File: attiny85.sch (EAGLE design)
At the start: 9 parts, among them U2 ATTINY85V-10SU

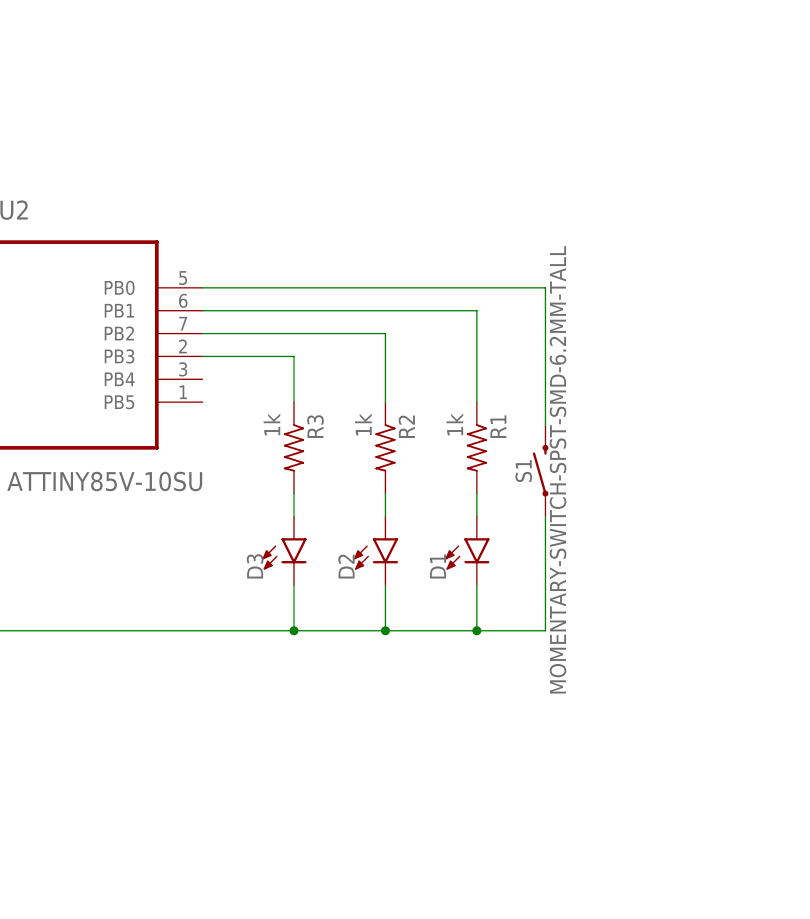
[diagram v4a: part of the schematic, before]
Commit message: Switching to using the "3" PWMs for the LEDs
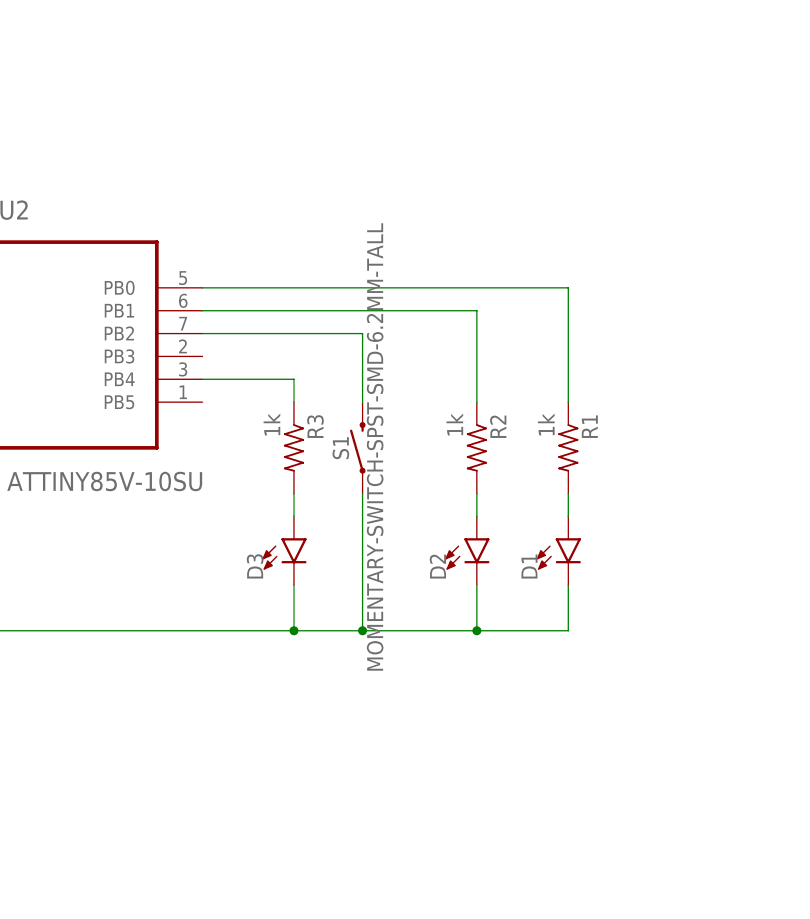
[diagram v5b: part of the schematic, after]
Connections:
- removed net N$8: R3.1, U2.PB3
- new net N$6: R3.1, U2.PB4
- net N$3: now also R1.1; no longer S1.2
- net N$4: now also R2.1; no longer R1.1
- net N$7: now also S1.2; no longer R2.1
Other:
- moved on the sheet: D1, D2, R1, R2, S1
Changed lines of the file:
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@@
 <instance part="FRAME1" gate="G$1" x="0" y="0"/>
 <instance part="FRAME1" gate="G$2" x="299.72" y="0"/>
-<instance part="R2" gate="G$1" x="93.98" y="185.42" rot="R270"/>
-<instance part="D2" gate="G$1" x="93.98" y="175.26"/>
+<instance part="R2" gate="G$1" x="104.14" y="185.42" rot="R270"/>
+<instance part="D2" gate="G$1" x="104.14" y="175.26"/>
 <instance part="R3" gate="G$1" x="83.82" y="185.42" rot="R270"/>
 <instance part="D3" gate="G$1" x="83.82" y="175.26"/>
 <instance part="BAT1" gate="G$1" x="30.48" y="198.12" rot="R90"/>
 <instance part="U2" gate="A" x="55.88" y="200.66"/>
-<instance part="R1" gate="G$1" x="104.14" y="185.42" rot="R270"/>
-<instance part="D1" gate="G$1" x="104.14" y="175.26"/>
-<instance part="S1" gate="G$1" x="111.76" y="182.88" rot="R90"/>
+<instance part="R1" gate="G$1" x="114.3" y="185.42" rot="R270"/>
+<instance part="D1" gate="G$1" x="114.3" y="175.26"/>
+<instance part="S1" gate="G$1" x="91.44" y="185.42" rot="R90"/>
 </instances>
 <busses>
@@
 <pinref part="R2" gate="G$1" pin="2"/>
 <pinref part="D2" gate="G$1" pin="A"/>
-<wire x1="93.98" y1="180.34" x2="93.98" y2="177.8" width="0.1524" layer="91"/>
+<wire x1="104.14" y1="180.34" x2="104.14" y2="177.8" width="0.1524" layer="91"/>
 </segment>
 </net>
@@
 <junction x="30.48" y="193.04"/>
 <pinref part="D1" gate="G$1" pin="C"/>
-<wire x1="104.14" y1="170.18" x2="104.14" y2="165.1" width="0.1524" layer="91"/>
+<wire x1="114.3" y1="170.18" x2="114.3" y2="165.1" width="0.1524" layer="91"/>
 <wire x1="30.48" y1="165.1" x2="83.82" y2="165.1" width="0.1524" layer="91"/>
 <pinref part="D3" gate="G$1" pin="C"/>
-<wire x1="83.82" y1="165.1" x2="93.98" y2="165.1" width="0.1524" layer="91"/>
-<wire x1="93.98" y1="165.1" x2="104.14" y2="165.1" width="0.1524" layer="91"/>
+<wire x1="83.82" y1="165.1" x2="91.44" y2="165.1" width="0.1524" layer="91"/>
+<wire x1="91.44" y1="165.1" x2="104.14" y2="165.1" width="0.1524" layer="91"/>
+<wire x1="104.14" y1="165.1" x2="114.3" y2="165.1" width="0.1524" layer="91"/>
 <wire x1="83.82" y1="170.18" x2="83.82" y2="165.1" width="0.1524" layer="91"/>
 <junction x="83.82" y="165.1"/>
 <pinref part="D2" gate="G$1" pin="C"/>
-<wire x1="93.98" y1="170.18" x2="93.98" y2="165.1" width="0.1524" layer="91"/>
-<junction x="93.98" y="165.1"/>
+<wire x1="104.14" y1="170.18" x2="104.14" y2="165.1" width="0.1524" layer="91"/>
+<junction x="104.14" y="165.1"/>
 <pinref part="S1" gate="G$1" pin="1"/>
-<wire x1="111.76" y1="177.8" x2="111.76" y2="165.1" width="0.1524" layer="91"/>
-<wire x1="111.76" y1="165.1" x2="104.14" y2="165.1" width="0.1524" layer="91"/>
-<junction x="104.14" y="165.1"/>
+<wire x1="91.44" y1="180.34" x2="91.44" y2="165.1" width="0.1524" layer="91"/>
+<junction x="91.44" y="165.1"/>
 </segment>
 </net>
@@
 <pinref part="R1" gate="G$1" pin="2"/>
 <pinref part="D1" gate="G$1" pin="A"/>
-<wire x1="104.14" y1="180.34" x2="104.14" y2="177.8" width="0.1524" layer="91"/>
+<wire x1="114.3" y1="180.34" x2="114.3" y2="177.8" width="0.1524" layer="91"/>
 </segment>
 </net>
@@
 </segment>
 </net>
+<net name="N$6" class="0">
+<segment>
+<pinref part="U2" gate="A" pin="PB4"/>
+<pinref part="R3" gate="G$1" pin="1"/>
+<wire x1="73.66" y1="193.04" x2="83.82" y2="193.04" width="0.1524" layer="91"/>
+<wire x1="83.82" y1="193.04" x2="83.82" y2="190.5" width="0.1524" layer="91"/>
+</segment>
+</net>
+<net name="N$3" class="0">
+<segment>
+<pinref part="U2" gate="A" pin="PB0"/>
+<pinref part="R1" gate="G$1" pin="1"/>
+<wire x1="73.66" y1="203.2" x2="114.3" y2="203.2" width="0.1524" layer="91"/>
+<wire x1="114.3" y1="203.2" x2="114.3" y2="190.5" width="0.1524" layer="91"/>
+</segment>
+</net>
 <net name="N$4" class="0">
 <segment>
 <pinref part="U2" gate="A" pin="PB1"/>
-<pinref part="R1" gate="G$1" pin="1"/>
+<pinref part="R2" gate="G$1" pin="1"/>
 <wire x1="73.66" y1="200.66" x2="104.14" y2="200.66" width="0.1524" layer="91"/>
 <wire x1="104.14" y1="200.66" x2="104.14" y2="190.5" width="0.1524" layer="91"/>
@@
 <segment>
 <pinref part="U2" gate="A" pin="PB2"/>
-<pinref part="R2" gate="G$1" pin="1"/>
-<wire x1="73.66" y1="198.12" x2="93.98" y2="198.12" width="0.1524" layer="91"/>
-<wire x1="93.98" y1="198.12" x2="93.98" y2="190.5" width="0.1524" layer="91"/>
+<pinref part="S1" gate="G$1" pin="2"/>
+<wire x1="73.66" y1="198.12" x2="91.44" y2="198.12" width="0.1524" layer="91"/>
+<wire x1="91.44" y1="198.12" x2="91.44" y2="190.5" width="0.1524" layer="91"/>
 </segment>
 </net>
-<net name="N$8" class="0">
-<segment>
-<pinref part="U2" gate="A" pin="PB3"/>
-<pinref part="R3" gate="G$1" pin="1"/>
-<wire x1="73.66" y1="195.58" x2="83.82" y2="195.58" width="0.1524" layer="91"/>
-<wire x1="83.82" y1="195.58" x2="83.82" y2="190.5" width="0.1524" layer="91"/>
-</segment>
-</net>
-<net name="N$3" class="0">
-<segment>
-<pinref part="U2" gate="A" pin="PB0"/>
-<pinref part="S1" gate="G$1" pin="2"/>
-<wire x1="73.66" y1="203.2" x2="111.76" y2="203.2" width="0.1524" layer="91"/>
-<wire x1="111.76" y1="203.2" x2="111.76" y2="187.96" width="0.1524" layer="91"/>
-</segment>
-</net>

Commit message: Using a smaller frame on the schematic
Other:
- moved on the sheet: BAT1, D1, D2, D3, R1, R2, R3, S1, U2
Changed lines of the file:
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@@
 </classes>
 <parts>
-<part name="FRAME1" library="frames" deviceset="TABL_L" device=""/>
 <part name="R2" library="adafruit" deviceset="R-US_" device="M1206" value="1k"/>
 <part name="D2" library="SparkFun-LED" deviceset="LED" device="1206"/>
@@
 <part name="D1" library="SparkFun-LED" deviceset="LED" device="1206"/>
 <part name="S1" library="SparkFun-Switches" deviceset="MOMENTARY-SWITCH-SPST" device="-SMD-6.2MM-TALL"/>
+<part name="FRAME1" library="frames" deviceset="A4L-LOC" device=""/>
 </parts>
 <sheets>
@@
 </plain>
 <instances>
+<instance part="R2" gate="G$1" x="93.98" y="137.16" rot="R270"/>
+<instance part="D2" gate="G$1" x="93.98" y="127"/>
+<instance part="R3" gate="G$1" x="73.66" y="137.16" rot="R270"/>
+<instance part="D3" gate="G$1" x="73.66" y="127"/>
+<instance part="BAT1" gate="G$1" x="20.32" y="149.86" rot="R90"/>
+<instance part="U2" gate="A" x="45.72" y="152.4"/>
+<instance part="R1" gate="G$1" x="104.14" y="137.16" rot="R270"/>
+<instance part="D1" gate="G$1" x="104.14" y="127"/>
+<instance part="S1" gate="G$1" x="81.28" y="137.16" rot="R90"/>
 <instance part="FRAME1" gate="G$1" x="0" y="0"/>
-<instance part="FRAME1" gate="G$2" x="299.72" y="0"/>
-<instance part="R2" gate="G$1" x="104.14" y="185.42" rot="R270"/>
-<instance part="D2" gate="G$1" x="104.14" y="175.26"/>
-<instance part="R3" gate="G$1" x="83.82" y="185.42" rot="R270"/>
-<instance part="D3" gate="G$1" x="83.82" y="175.26"/>
-<instance part="BAT1" gate="G$1" x="30.48" y="198.12" rot="R90"/>
-<instance part="U2" gate="A" x="55.88" y="200.66"/>
-<instance part="R1" gate="G$1" x="114.3" y="185.42" rot="R270"/>
-<instance part="D1" gate="G$1" x="114.3" y="175.26"/>
-<instance part="S1" gate="G$1" x="91.44" y="185.42" rot="R90"/>
 </instances>
 <busses>
@@
 <pinref part="R2" gate="G$1" pin="2"/>
 <pinref part="D2" gate="G$1" pin="A"/>
-<wire x1="104.14" y1="180.34" x2="104.14" y2="177.8" width="0.1524" layer="91"/>
+<wire x1="93.98" y1="132.08" x2="93.98" y2="129.54" width="0.1524" layer="91"/>
 </segment>
 </net>
@@
 <pinref part="BAT1" gate="G$1" pin="-"/>
 <pinref part="U2" gate="A" pin="GND"/>
-<wire x1="38.1" y1="193.04" x2="30.48" y2="193.04" width="0.1524" layer="91"/>
-<wire x1="30.48" y1="193.04" x2="30.48" y2="165.1" width="0.1524" layer="91"/>
-<junction x="30.48" y="193.04"/>
+<wire x1="27.94" y1="144.78" x2="20.32" y2="144.78" width="0.1524" layer="91"/>
+<wire x1="20.32" y1="144.78" x2="20.32" y2="116.84" width="0.1524" layer="91"/>
+<junction x="20.32" y="144.78"/>
 <pinref part="D1" gate="G$1" pin="C"/>
-<wire x1="114.3" y1="170.18" x2="114.3" y2="165.1" width="0.1524" layer="91"/>
-<wire x1="30.48" y1="165.1" x2="83.82" y2="165.1" width="0.1524" layer="91"/>
+<wire x1="104.14" y1="121.92" x2="104.14" y2="116.84" width="0.1524" layer="91"/>
+<wire x1="20.32" y1="116.84" x2="73.66" y2="116.84" width="0.1524" layer="91"/>
 <pinref part="D3" gate="G$1" pin="C"/>
-<wire x1="83.82" y1="165.1" x2="91.44" y2="165.1" width="0.1524" layer="91"/>
-<wire x1="91.44" y1="165.1" x2="104.14" y2="165.1" width="0.1524" layer="91"/>
-<wire x1="104.14" y1="165.1" x2="114.3" y2="165.1" width="0.1524" layer="91"/>
-<wire x1="83.82" y1="170.18" x2="83.82" y2="165.1" width="0.1524" layer="91"/>
-<junction x="83.82" y="165.1"/>
+<wire x1="73.66" y1="116.84" x2="81.28" y2="116.84" width="0.1524" layer="91"/>
+<wire x1="81.28" y1="116.84" x2="93.98" y2="116.84" width="0.1524" layer="91"/>
+<wire x1="93.98" y1="116.84" x2="104.14" y2="116.84" width="0.1524" layer="91"/>
+<wire x1="73.66" y1="121.92" x2="73.66" y2="116.84" width="0.1524" layer="91"/>
+<junction x="73.66" y="116.84"/>
 <pinref part="D2" gate="G$1" pin="C"/>
-<wire x1="104.14" y1="170.18" x2="104.14" y2="165.1" width="0.1524" layer="91"/>
-<junction x="104.14" y="165.1"/>
+<wire x1="93.98" y1="121.92" x2="93.98" y2="116.84" width="0.1524" layer="91"/>
+<junction x="93.98" y="116.84"/>
 <pinref part="S1" gate="G$1" pin="1"/>
-<wire x1="91.44" y1="180.34" x2="91.44" y2="165.1" width="0.1524" layer="91"/>
-<junction x="91.44" y="165.1"/>
+<wire x1="81.28" y1="132.08" x2="81.28" y2="116.84" width="0.1524" layer="91"/>
+<junction x="81.28" y="116.84"/>
 </segment>
 </net>
@@
 <pinref part="R3" gate="G$1" pin="2"/>
 <pinref part="D3" gate="G$1" pin="A"/>
-<wire x1="83.82" y1="180.34" x2="83.82" y2="177.8" width="0.1524" layer="91"/>
+<wire x1="73.66" y1="132.08" x2="73.66" y2="129.54" width="0.1524" layer="91"/>
 </segment>
 </net>
@@
 <pinref part="R1" gate="G$1" pin="2"/>
 <pinref part="D1" gate="G$1" pin="A"/>
-<wire x1="114.3" y1="180.34" x2="114.3" y2="177.8" width="0.1524" layer="91"/>
+<wire x1="104.14" y1="132.08" x2="104.14" y2="129.54" width="0.1524" layer="91"/>
 </segment>
 </net>
@@
 <segment>
 <pinref part="BAT1" gate="G$1" pin="+"/>
-<junction x="27.94" y="203.2"/>
+<junction x="17.78" y="154.94"/>
 <pinref part="BAT1" gate="G$1" pin="+1"/>
 <pinref part="U2" gate="A" pin="VCC"/>
-<wire x1="38.1" y1="203.2" x2="33.02" y2="203.2" width="0.1524" layer="91"/>
-<junction x="33.02" y="203.2"/>
-<wire x1="33.02" y1="203.2" x2="27.94" y2="203.2" width="0.1524" layer="91"/>
-<wire x1="27.94" y1="203.2" x2="30.48" y2="203.2" width="0.1524" layer="91"/>
+<wire x1="27.94" y1="154.94" x2="22.86" y2="154.94" width="0.1524" layer="91"/>
+<junction x="22.86" y="154.94"/>
+<wire x1="22.86" y1="154.94" x2="17.78" y2="154.94" width="0.1524" layer="91"/>
+<wire x1="17.78" y1="154.94" x2="20.32" y2="154.94" width="0.1524" layer="91"/>
 </segment>
 </net>
@@
 <pinref part="U2" gate="A" pin="PB4"/>
 <pinref part="R3" gate="G$1" pin="1"/>
-<wire x1="73.66" y1="193.04" x2="83.82" y2="193.04" width="0.1524" layer="91"/>
-<wire x1="83.82" y1="193.04" x2="83.82" y2="190.5" width="0.1524" layer="91"/>
+<wire x1="63.5" y1="144.78" x2="73.66" y2="144.78" width="0.1524" layer="91"/>
+<wire x1="73.66" y1="144.78" x2="73.66" y2="142.24" width="0.1524" layer="91"/>
 </segment>
 </net>
@@
 <pinref part="U2" gate="A" pin="PB0"/>
 <pinref part="R1" gate="G$1" pin="1"/>
-<wire x1="73.66" y1="203.2" x2="114.3" y2="203.2" width="0.1524" layer="91"/>
-<wire x1="114.3" y1="203.2" x2="114.3" y2="190.5" width="0.1524" layer="91"/>
+<wire x1="63.5" y1="154.94" x2="104.14" y2="154.94" width="0.1524" layer="91"/>
+<wire x1="104.14" y1="154.94" x2="104.14" y2="142.24" width="0.1524" layer="91"/>
 </segment>
 </net>
@@
 <pinref part="U2" gate="A" pin="PB1"/>
 <pinref part="R2" gate="G$1" pin="1"/>
-<wire x1="73.66" y1="200.66" x2="104.14" y2="200.66" width="0.1524" layer="91"/>
-<wire x1="104.14" y1="200.66" x2="104.14" y2="190.5" width="0.1524" layer="91"/>
+<wire x1="63.5" y1="152.4" x2="93.98" y2="152.4" width="0.1524" layer="91"/>
+<wire x1="93.98" y1="152.4" x2="93.98" y2="142.24" width="0.1524" layer="91"/>
 </segment>
 </net>
@@
 <pinref part="U2" gate="A" pin="PB2"/>
 <pinref part="S1" gate="G$1" pin="2"/>
-<wire x1="73.66" y1="198.12" x2="91.44" y2="198.12" width="0.1524" layer="91"/>
-<wire x1="91.44" y1="198.12" x2="91.44" y2="190.5" width="0.1524" layer="91"/>
+<wire x1="63.5" y1="149.86" x2="81.28" y2="149.86" width="0.1524" layer="91"/>
+<wire x1="81.28" y1="149.86" x2="81.28" y2="142.24" width="0.1524" layer="91"/>
 </segment>
 </net>
